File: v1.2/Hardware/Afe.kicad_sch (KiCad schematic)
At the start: 44 parts, among them Q15 MMBT3904, Q16 MMBT3904, U10 ACPL-7900, U13 L78L05_SOT89, U3 MCP6022, U4 ACPL-7900, U5 TL431LP

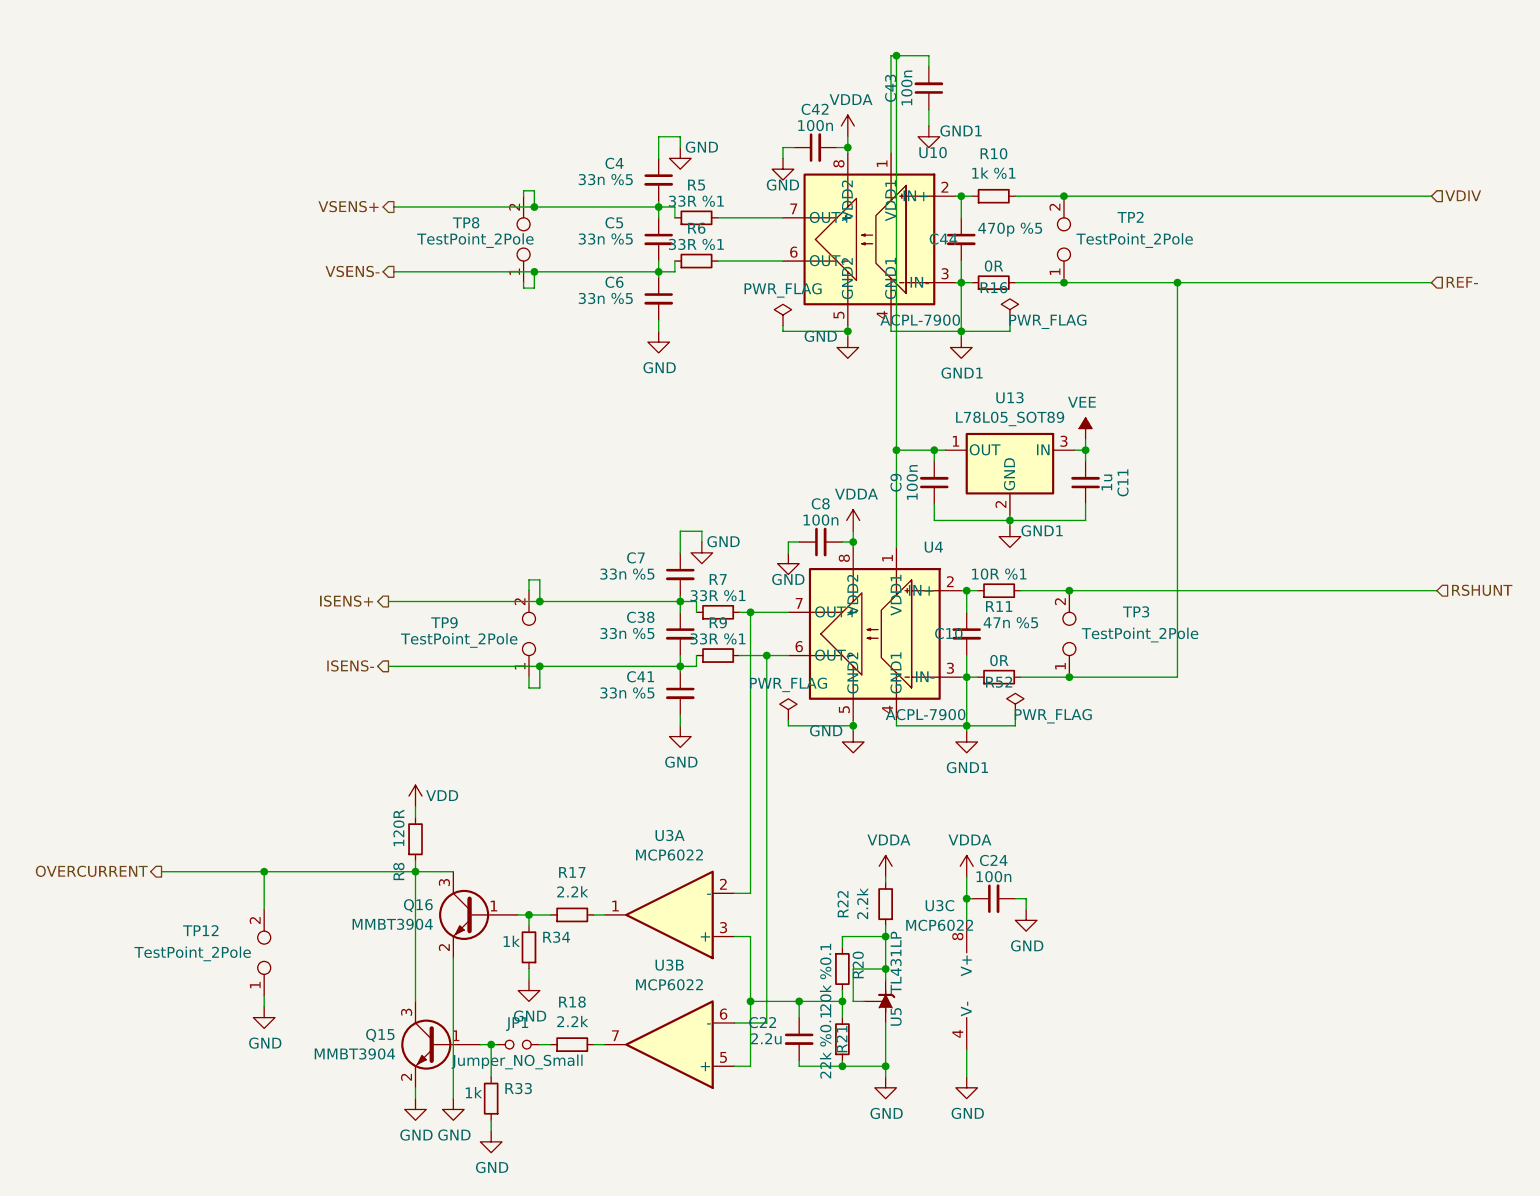
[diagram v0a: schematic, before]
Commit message: Addition of firmware to v1.2(not tested)
+Addition of power tracking(with duty cycle control).
+Addition of resonance freq tracking(via proprietary algorithm relied on active and reactive power measurements)
+Quality factor monitoring
+Power boost when loaded(idle and loaded modes)
+Much better frequency resolution(less than 1Hz)
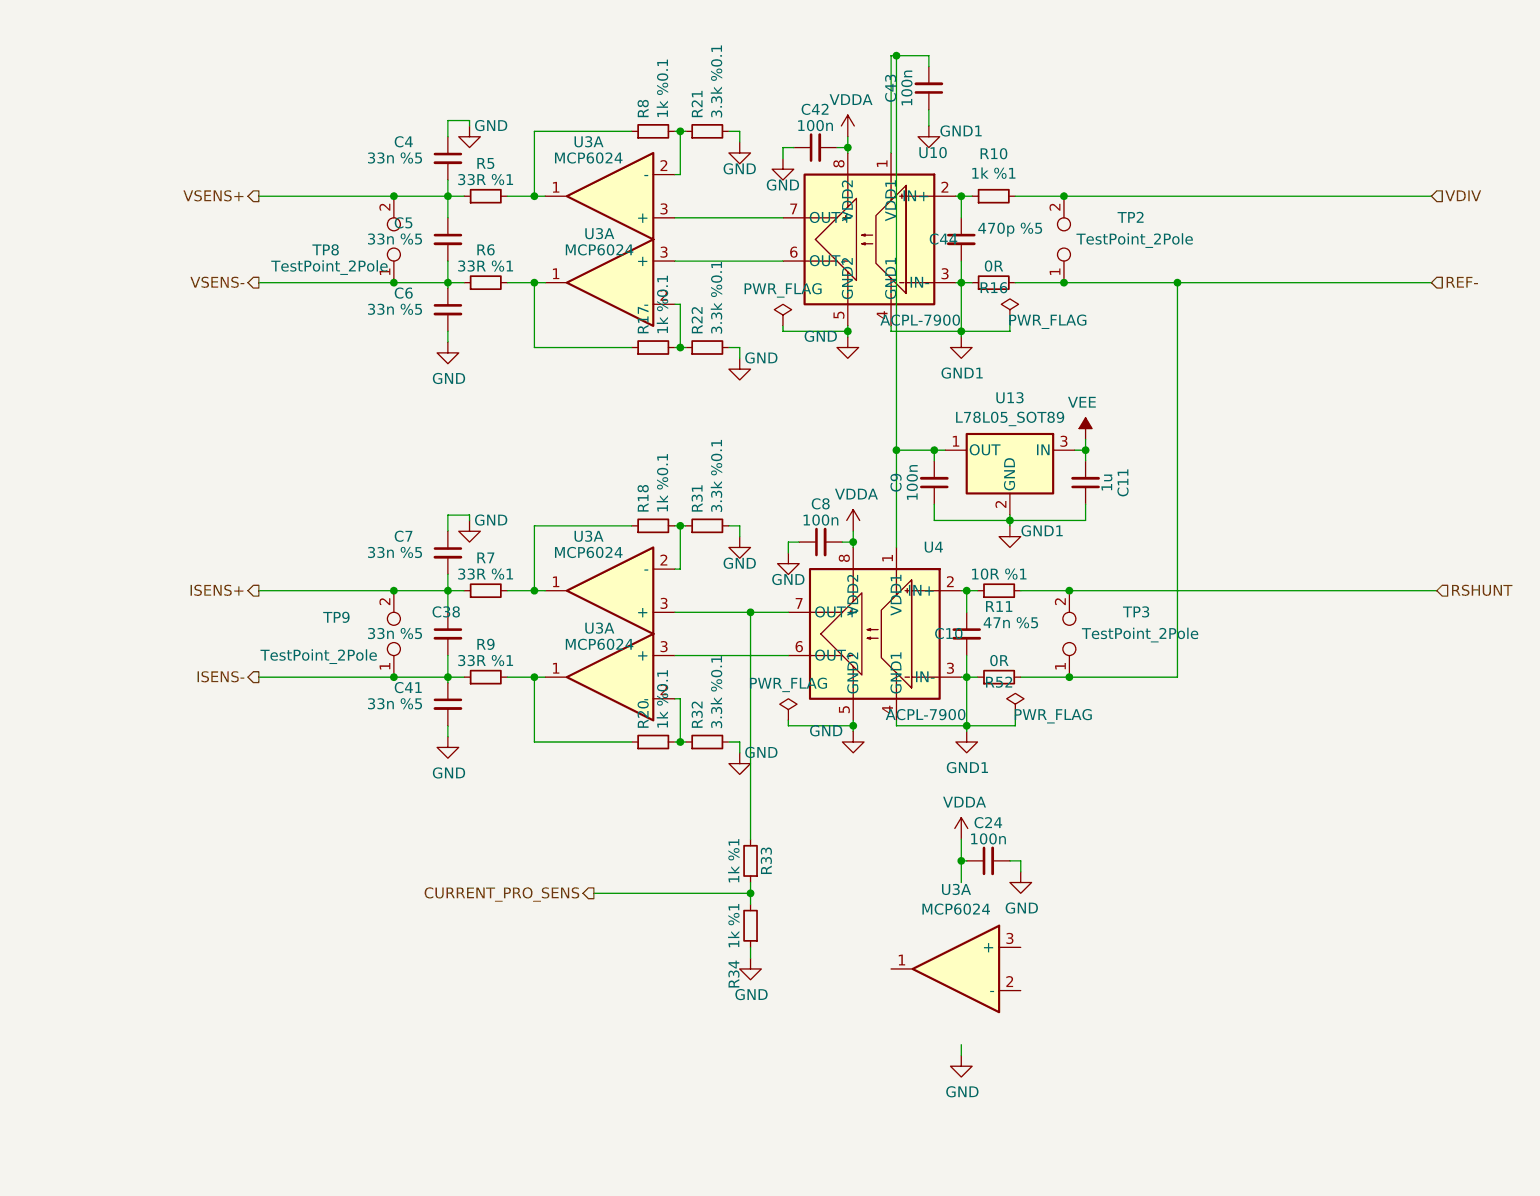
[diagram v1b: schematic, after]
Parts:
- removed C22: 2.2u, Capacitor_SMD:C_0805_2012Metric, symbol Device:C_Small
- removed JP1: Jumper_NO_Small, Connector_PinHeader_2.54mm:PinHeader_1x02_P2.54mm_Vertical, symbol Device:Jumper_NO_Small
- removed Q15, Q16: MMBT3904, Package_TO_SOT_SMD:SOT-23, symbol Transistor_BJT:MMBT3904
- removed TP12: TestPoint_2Pole, Connector_PinHeader_2.54mm:PinHeader_1x02_P2.54mm_Vertical, symbol Connector:TestPoint_2Pole
- removed unit 1 of U3
- removed unit 2 of U3
- removed U5: TL431LP, Package_TO_SOT_SMD:SOT-23, symbol Reference_Voltage:TL431DBZ
- added R31, R32: 3.3k %0.1, Resistor_SMD:R_0805_2012Metric, symbol Device:R_Small
- added U3 (x4): MCP6024, Package_SO:SOIC-14_3.9x8.7mm_P1.27mm, symbol oe_opamp:MCP6024
- C38, C4, C41, C5, C6, C7: footprint Capacitor_SMD:C_0603_1608Metric -> Capacitor_SMD:C_0805_2012Metric; Price 0.13651TL -> 0.13655TL
- R17, R18: value 2.2k -> 1k %0.1; Link https://ozdisan.com/passive-components/resistors/smt-smd-and-chip-resistors/0805S8J0222T5E -> https://ozdisan.com/passive-components/resistors/smt-smd-and-chip-resistors/0805S8F1001T5E; Price 0.01504TL -> 0.01964TL
- R20: value 20k %0.1 -> 1k %0.1; Link https://ozdisan.com/passive-components/resistors/smt-smd-and-chip-resistors/TC0525B2002T5F -> https://ozdisan.com/passive-components/resistors/smt-smd-and-chip-resistors/0805S8F1001T5E; Price 0.61119TL -> 0.01964TL
- R21: value 22k %0.1 -> 3.3k %0.1; Link https://ozdisan.com/passive-components/resistors/smt-smd-and-chip-resistors/TC0525B2202T5F -> https://ozdisan.com/passive-components/resistors/smt-smd-and-chip-resistors/TC0525B3301T5F; Price 0.61718TL -> 0.61992TL
- R22: value 2.2k -> 3.3k %0.1; Link https://ozdisan.com/passive-components/resistors/smt-smd-and-chip-resistors/0805S8J0222T5E -> https://ozdisan.com/passive-components/resistors/smt-smd-and-chip-resistors/TC0525B3301T5F; Price 0.01504TL -> 0.61992TL
- R33, R34: value 1k -> 1k %1; Link https://ozdisan.com/passive-components/resistors/smt-smd-and-chip-resistors/CQ05S8J0102T5E -> https://ozdisan.com/passive-components/resistors/smt-smd-and-chip-resistors/0805S8F1001T5E; Price 0.02034TL -> 0.01963TL
- R5, R6, R7, R9: Link https://ozdisan.com/passive-components/resistors/smt-smd-and-chip-resistors/CQ05S8F330JT5E -> https://ozdisan.com/passive-components/resistors/smt-smd-and-chip-resistors/0805S8F330JT5E; Price 0.02588TL -> 0.01964TL
- R8: value 120R -> 1k %0.1; Link https://ozdisan.com/passive-components/resistors/smt-smd-and-chip-resistors/0805S8J0121T5E -> https://ozdisan.com/passive-components/resistors/smt-smd-and-chip-resistors/0805S8F1001T5E; Price 0.01492TL -> 0.01964TL
- U3: value MCP6022 -> MCP6024; footprint Package_SO:SOIC-8_3.9x4.9mm_P1.27mm -> Package_SO:SOIC-14_3.9x8.7mm_P1.27mm; symbol Amplifier_Operational:MCP6022 -> oe_opamp:MCP6024; Price 11.41088TL -> 11.51570TL
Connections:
- net OVERCURRENT is gone; now on an unnamed net: R8.1
- net GND: now also R21.2, R22.2, R31.2, R32.2; no longer R21.1, R33.1, U3.4 (V-)
- net VDDA: no longer R22.2, U3.8 (V+)
- net at R22.1: now also R17.2, U3.2 (-); no longer R20.1
- net at U10.6 (OUT-): now also U3.3 (+); no longer R6.2
- net at R5.2: now also U3.1; no longer U10.7 (OUT+)
- net at R17.1: now also R6.2, U3.1; no longer R34.2
- net at R7.2: now also R18.1, U3.1; no longer U4.7 (OUT+)
- net at R20.2: now also R32.1, U3.2 (-); no longer R21.2
- net at R33.2: now also U4.7 (OUT+), U3.3 (+)
- net at R9.2: now also R20.1, U3.1; no longer U4.6 (OUT-)
- net at R18.2: now also R31.1, U3.2 (-)
- net VDD: no longer names the net of R8.2
- net VDD: now also R21.1, U3.2 (-)
- new net: U10.7 (OUT+), U3.3 (+)
- new net: U3.3 (+), U4.6 (OUT-)
- new net CURRENT_PRO_SENS: R33.1, R34.2
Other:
- moved on the sheet: C24, TP8

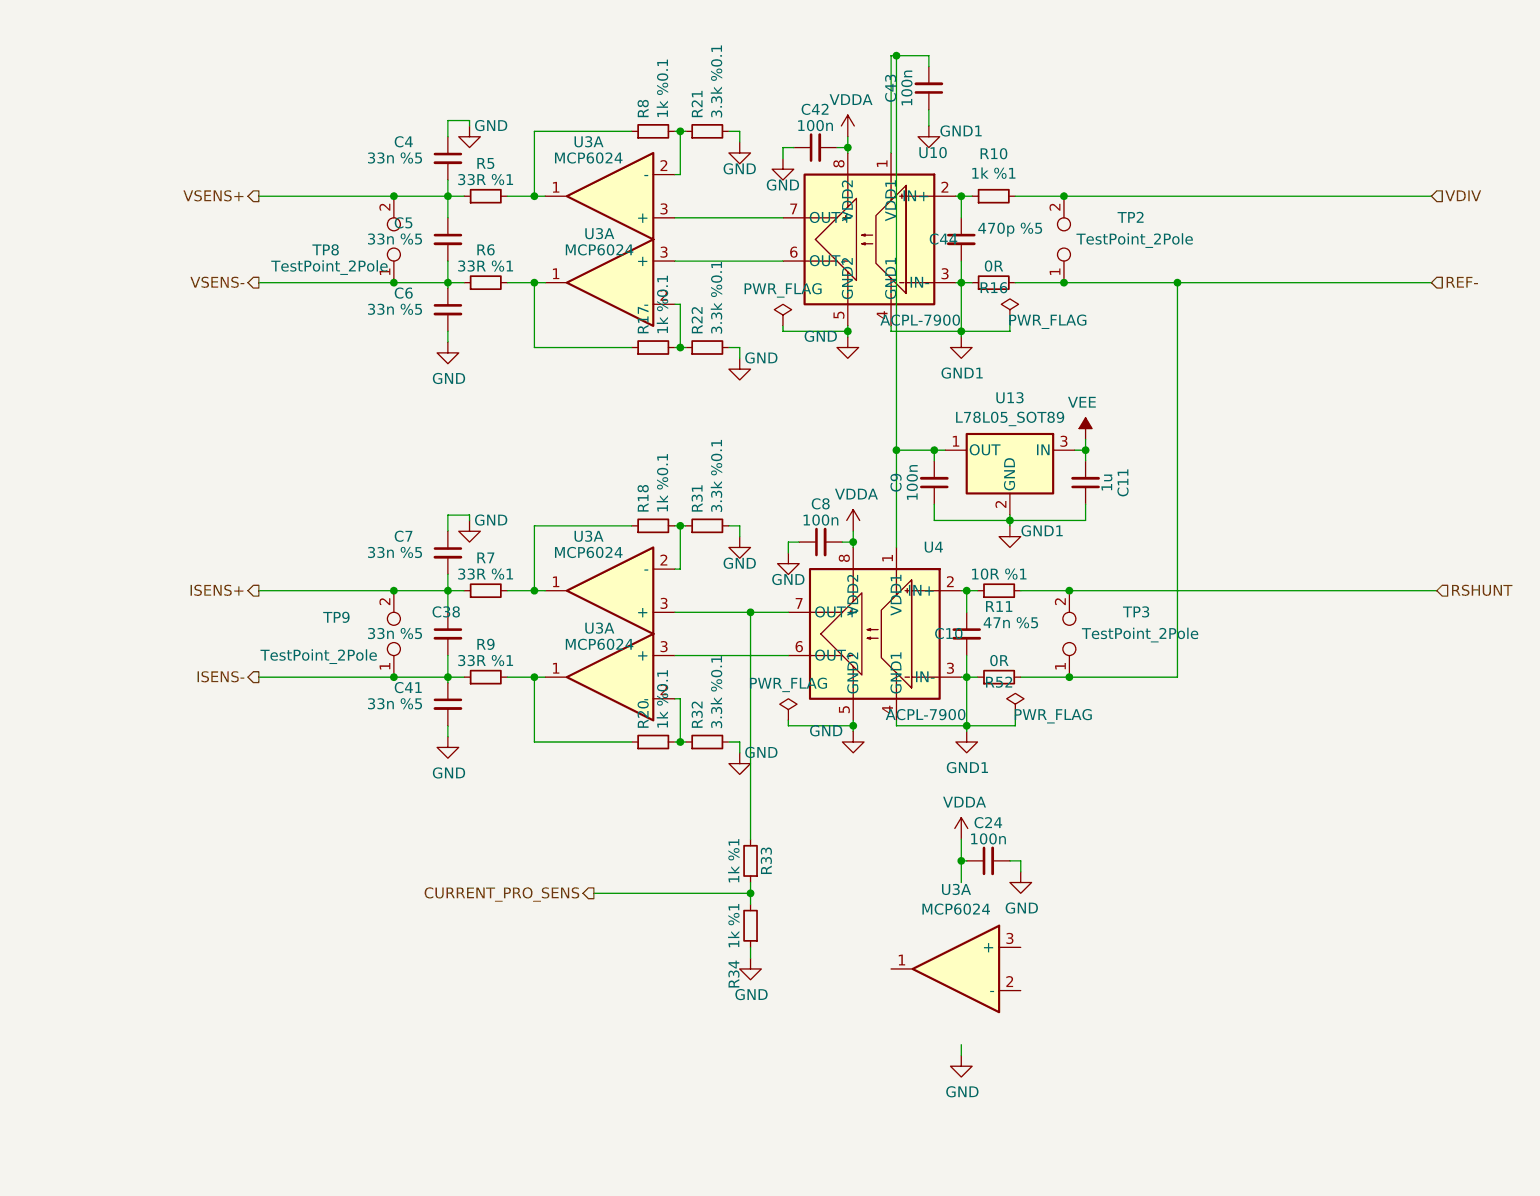
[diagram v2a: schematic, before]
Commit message: Redesign.
+Cli interface.
+Modularity improvement(complex number and pid modules created)
+Range change.
+Core-Lattice seperated. 
+Improvement of the control function
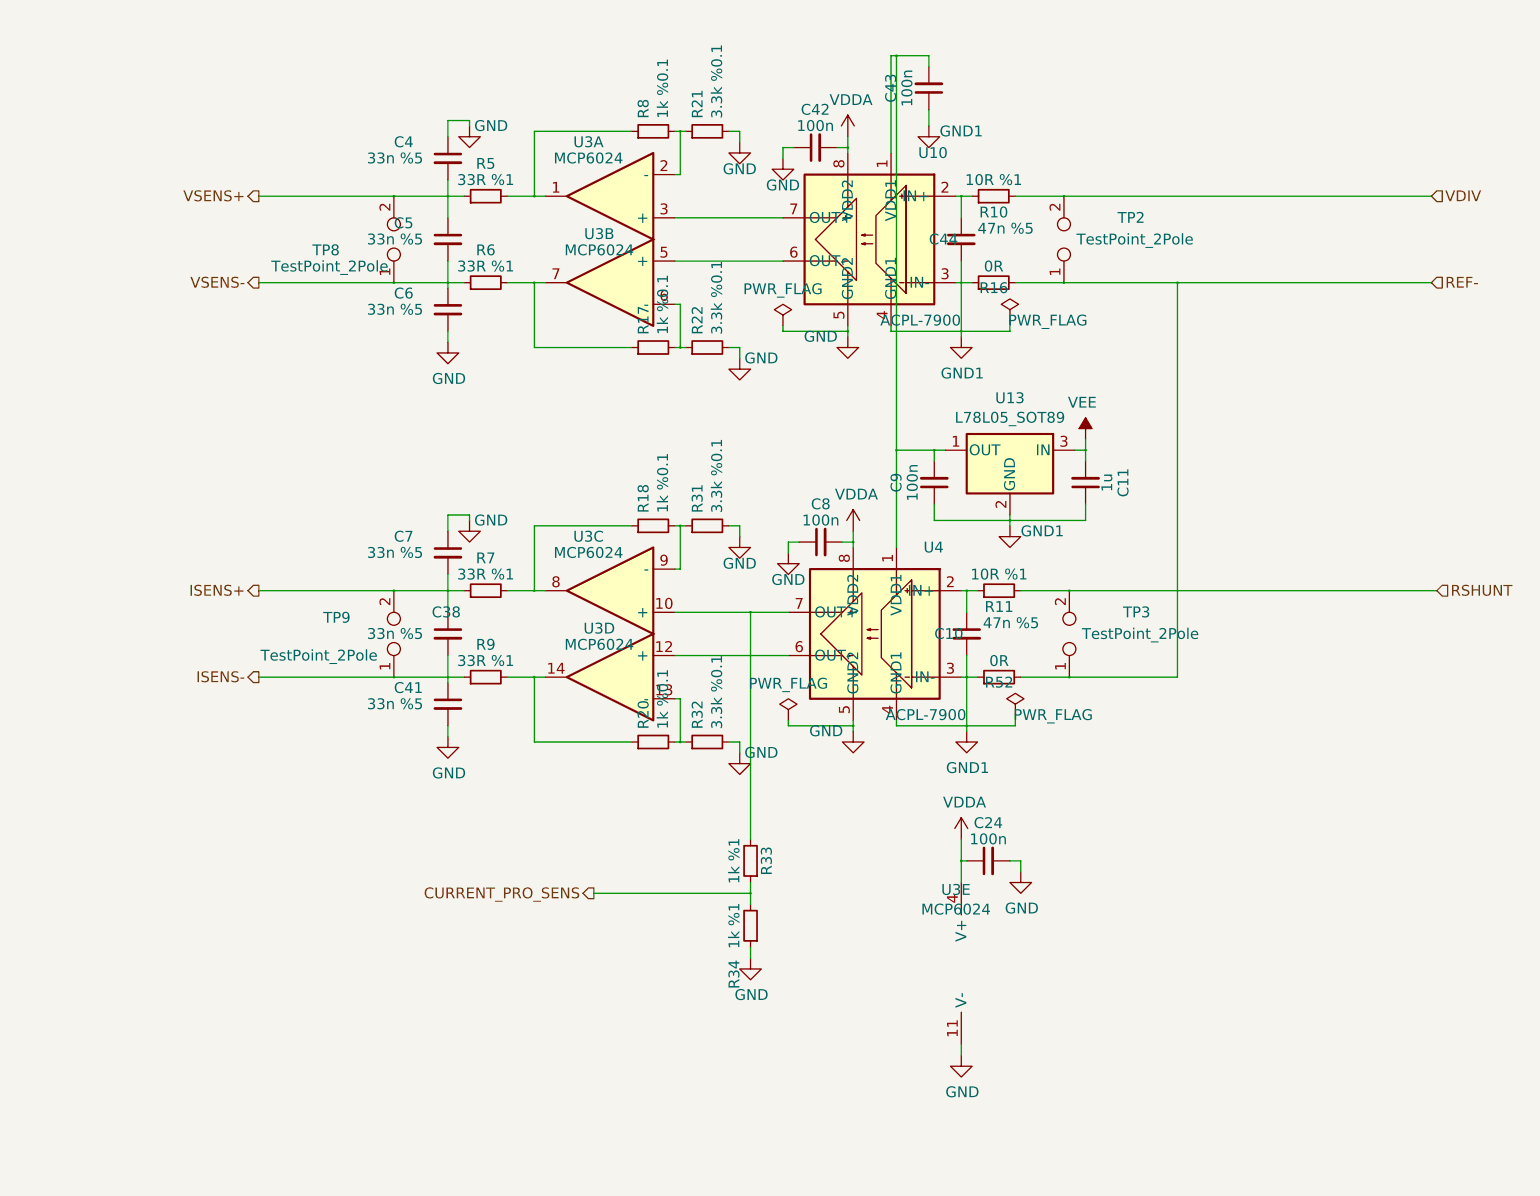
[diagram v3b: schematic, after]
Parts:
- C44: value 470p %5 -> 47n %5; Link https://ozdisan.com/passive-components/capacitors/smt-smd-and-mlcc-capacitors/CL21C471JBANNNC -> https://ozdisan.com/passive-components/capacitors/smt-smd-and-mlcc-capacitors/CL21B473JBCNNNC; Price 0.08961TL -> 0.13651TL
- R10: value 1k %1 -> 10R %1; Link https://ozdisan.com/passive-components/resistors/smt-smd-and-chip-resistors/0805S8F1001T5E -> https://ozdisan.com/passive-components/resistors/smt-smd-and-chip-resistors/TC0550F100JT5F; Price 0.01963TL -> 0.17671TL
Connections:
- net GND: now also U3.11 (V-)
- net VDDA: now also U3.4 (V+)
- net at R20.2, R32.1: now also U3.13 (-); no longer U3.2 (-)
- net at U10.6 (OUT-): now also U3.5 (+); no longer U3.3 (+)
- net at R18.1, R7.2: now also U3.8; no longer U3.1
- net at R18.2, R31.1: now also U3.9 (-); no longer U3.2 (-)
- net at R17.1, R6.2: now also U3.7; no longer U3.1
- net at R17.2, R22.1: now also U3.6 (-); no longer U3.2 (-)
- net at R33.2, U4.7 (OUT+): now also U3.10 (+); no longer U3.3 (+)
- net at R20.1, R9.2: now also U3.14; no longer U3.1
- net at U4.6 (OUT-): now also U3.12 (+); no longer U3.3 (+)
